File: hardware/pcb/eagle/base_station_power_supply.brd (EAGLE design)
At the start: 30 x 68.5 mm, 17 parts, among them CON1 POWER_JACKPTH, IC1 MB16S-TP

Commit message: Increased width of 24V track
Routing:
- net N$8: track 17.9 -> 22.9 mm
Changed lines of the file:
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@@
 </signal>
 <signal name="+24V">
-<wire x1="2.5" y1="8.8" x2="2.5" y2="40" width="1.016" layer="16"/>
-<wire x1="2.5" y1="8.8" x2="5.5" y2="8.8" width="1.016" layer="16"/>
+<wire x1="2.5" y1="8.8" x2="2.5" y2="44.5" width="2.1844" layer="16"/>
+<wire x1="2.5" y1="8.8" x2="5.5" y2="8.8" width="2.1844" layer="16"/>
 <contactref element="IC1" pad="+"/>
 <contactref element="D1" pad="C"/>
 <contactref element="C4" pad="1"/>
 <contactref element="C1" pad="+"/>
-<wire x1="5.5" y1="8.8" x2="26.84" y2="8.8" width="1.016" layer="16"/>
+<wire x1="5.5" y1="8.8" x2="26.84" y2="8.8" width="2.1844" layer="16"/>
 <wire x1="18" y1="13.1" x2="14" y2="13.1" width="1.016" layer="16"/>
 <contactref element="F1" pad="2"/>
@@
 <wire x1="14" y1="13.1" x2="9.5" y2="13.1" width="1.016" layer="16"/>
 <wire x1="9.5" y1="13.1" x2="9.5" y2="13.05" width="1.016" layer="16"/>
-<wire x1="22.8" y1="52.45" x2="22.8" y2="49.5" width="0.8128" layer="16"/>
-<wire x1="22.8" y1="49.5" x2="20.3" y2="47" width="0.8128" layer="16"/>
-<wire x1="20.3" y1="47" x2="5" y2="47" width="0.8128" layer="16"/>
-<wire x1="5" y1="47" x2="2.5" y2="44.5" width="0.8128" layer="16"/>
-<wire x1="2.5" y1="44.5" x2="2.5" y2="40" width="0.8128" layer="16"/>
+<wire x1="22.8" y1="52.45" x2="22.8" y2="50.5" width="0.8128" layer="16"/>
+<wire x1="22.8" y1="50.5" x2="22.8" y2="49" width="2.1844" layer="16"/>
+<wire x1="22.8" y1="49" x2="20.8" y2="47" width="2.1844" layer="16"/>
+<wire x1="20.8" y1="47" x2="5" y2="47" width="2.1844" layer="16"/>
+<wire x1="5" y1="47" x2="2.5" y2="44.5" width="2.1844" layer="16"/>
 <contactref element="CON2" pad="1"/>
 <contactref element="CON4" pad="3"/>
-<wire x1="28.5" y1="10.96" x2="26.84" y2="8.8" width="1.016" layer="16"/>
+<wire x1="28.5" y1="10.96" x2="26.84" y2="8.8" width="1.4224" layer="16"/>
 <wire x1="22.8" y1="52.45" x2="24" y2="52.45" width="0.8128" layer="16"/>
-<wire x1="24" y1="52.45" x2="25" y2="53.45" width="0.8128" layer="16"/>
-<wire x1="25" y1="53.45" x2="25" y2="56.54" width="0.8128" layer="16"/>
-<wire x1="25" y1="56.54" x2="26" y2="57.54" width="0.8128" layer="16"/>
-<wire x1="26" y1="57.54" x2="28.5" y2="57.54" width="0.8128" layer="16"/>
+<wire x1="24" y1="52.45" x2="25" y2="53.45" width="1.016" layer="16"/>
+<wire x1="25" y1="53.45" x2="25" y2="56.54" width="1.6764" layer="16"/>
+<wire x1="25" y1="56.54" x2="26" y2="57.54" width="1.6764" layer="16"/>
+<wire x1="26" y1="57.54" x2="28.5" y2="57.54" width="1.27" layer="16"/>
 </signal>
 <signal name="S$41">
@@
 <via x="17.5" y="55" extent="1-16" drill="0.6"/>
 <via x="15" y="52.5" extent="1-16" drill="0.6"/>
-<via x="17.5" y="63" extent="1-16" drill="0.6"/>
-<via x="15" y="63" extent="1-16" drill="0.6"/>
-<via x="12.5" y="63" extent="1-16" drill="0.6"/>
 <via x="10" y="63" extent="1-16" drill="0.6"/>
 <via x="7.5" y="60.5" extent="1-16" drill="0.6"/>
@@
 <via x="2.5" y="55.5" extent="1-16" drill="0.6"/>
 <via x="2.5" y="53" extent="1-16" drill="0.6"/>
-<via x="20" y="63" extent="1-16" drill="0.6"/>
 <via x="27.5" y="29" extent="1-16" drill="0.6"/>
 <via x="27.5" y="26.5" extent="1-16" drill="0.6"/>
@@
 <contactref element="CON1" pad="GND"/>
 <contactref element="D1A" pad="1"/>
-<wire x1="18.5" y1="60.35" x2="12.55" y2="60.35" width="0.8128" layer="16"/>
-<wire x1="12.55" y1="60.35" x2="7.7" y2="55.5" width="0.8128" layer="16"/>
-<wire x1="22.8" y1="58.55" x2="21" y2="60.35" width="0.8128" layer="16"/>
-<wire x1="21" y1="60.35" x2="18.5" y2="60.35" width="0.8128" layer="16"/>
+<wire x1="18.5" y1="60.35" x2="18.5" y2="62.5" width="0.8128" layer="16"/>
+<wire x1="18.5" y1="62.5" x2="14.7" y2="62.5" width="2.1844" layer="16"/>
+<wire x1="14.7" y1="62.5" x2="7.7" y2="55.5" width="2.1844" layer="16"/>
+<wire x1="22.8" y1="58.55" x2="22.8" y2="60.5" width="1.016" layer="16"/>
+<wire x1="22.8" y1="60.5" x2="20.8" y2="62.5" width="2.1844" layer="16"/>
+<wire x1="20.8" y1="62.5" x2="18.5" y2="62.5" width="2.1844" layer="16"/>
 </signal>
 <signal name="N$2">

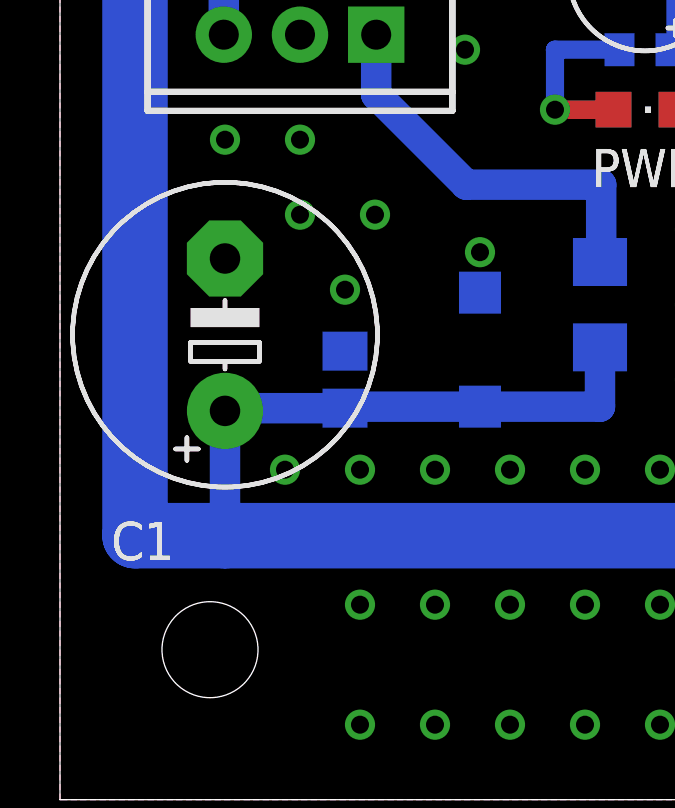
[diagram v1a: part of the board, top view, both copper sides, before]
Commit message: Moved C1 down 1.5mm to increase clearance between capacitor and regulator
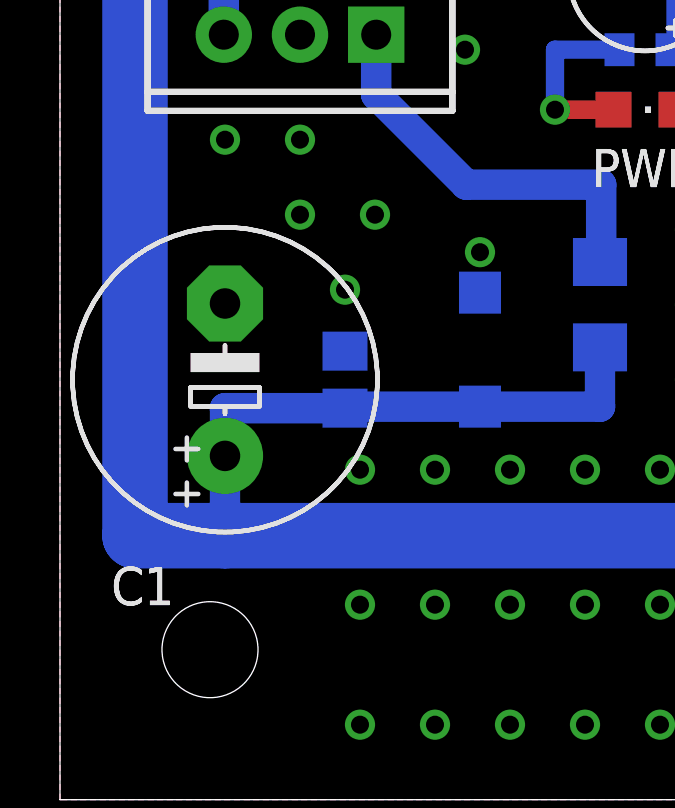
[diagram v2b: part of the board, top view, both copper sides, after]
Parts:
- moved C1 1.50 mm to (5.50, 14.0)
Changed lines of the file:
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@@
 <wire x1="30" y1="68.5" x2="30" y2="0" width="0" layer="20"/>
 <wire x1="30" y1="68.5" x2="0" y2="68.5" width="0" layer="20"/>
-<wire x1="5.499996875" y1="14.357003125" x2="5.499996875" y2="14.611003125" width="0.1524" layer="121"/>
-<wire x1="5.499996875" y1="14.611003125" x2="6.642996875" y2="14.611003125" width="0.1524" layer="121"/>
-<wire x1="6.642996875" y1="14.611003125" x2="6.642996875" y2="15.246003125" width="0.1524" layer="121"/>
-<wire x1="6.642996875" y1="15.246003125" x2="4.356996875" y2="15.246003125" width="0.1524" layer="121"/>
-<wire x1="4.356996875" y1="15.246003125" x2="4.356996875" y2="14.611003125" width="0.1524" layer="121"/>
-<wire x1="4.356996875" y1="14.611003125" x2="5.499996875" y2="14.611003125" width="0.1524" layer="121"/>
-<wire x1="5.499996875" y1="16.135003125" x2="5.499996875" y2="16.643003125" width="0.1524" layer="121"/>
+<wire x1="5.499996875" y1="12.857003125" x2="5.499996875" y2="13.111003125" width="0.1524" layer="121"/>
+<wire x1="5.499996875" y1="13.111003125" x2="6.642996875" y2="13.111003125" width="0.1524" layer="121"/>
+<wire x1="6.642996875" y1="13.111003125" x2="6.642996875" y2="13.746003125" width="0.1524" layer="121"/>
+<wire x1="6.642996875" y1="13.746003125" x2="4.356996875" y2="13.746003125" width="0.1524" layer="121"/>
+<wire x1="4.356996875" y1="13.746003125" x2="4.356996875" y2="13.111003125" width="0.1524" layer="121"/>
+<wire x1="4.356996875" y1="13.111003125" x2="5.499996875" y2="13.111003125" width="0.1524" layer="121"/>
+<wire x1="5.499996875" y1="14.635003125" x2="5.499996875" y2="15.143003125" width="0.1524" layer="121"/>
 <wire x1="3.848996875" y1="11.690003125" x2="4.610996875" y2="11.690003125" width="0.1524" layer="121"/>
 <wire x1="4.229996875" y1="12.071003125" x2="4.229996875" y2="11.309003125" width="0.1524" layer="121"/>
-<circle x="5.499996875" y="15.500003125" radius="5.08" width="0.1524" layer="121"/>
-<rectangle x1="5.182496875" y1="14.928503125" x2="5.817496875" y2="17.214503125" layer="121" rot="R90"/>
-<text x="3.80099375" y="9.2568125" size="1.27" layer="121" font="vector" ratio="10" rot="R180">C1</text>
+<circle x="5.499996875" y="14.000003125" radius="5.08" width="0.1524" layer="121"/>
+<rectangle x1="5.182496875" y1="13.428503125" x2="5.817496875" y2="15.714503125" layer="121" rot="R90"/>
+<text x="3.80099375" y="7.7568125" size="1.27" layer="121" font="vector" ratio="10" rot="R180">C1</text>
 <wire x1="20.769996875" y1="25.72200625" x2="20.261996875" y2="25.72200625" width="0.1524" layer="121"/>
 <wire x1="20.515996875" y1="25.97600625" x2="20.515996875" y2="25.46800625" width="0.1524" layer="121"/>
@@
 <attribute name="VALUE" x="18.865" y="27.54" size="1.27" layer="28" rot="MR180"/>
 </element>
-<element name="C1" library="rcl" package="E5-10,5" value="100uF" x="5.5" y="15.5" smashed="yes" rot="R90">
-<attribute name="NAME" x="3.801" y="9.2568" size="1.27" layer="25" font="vector" ratio="10" rot="R180"/>
-<attribute name="VALUE" x="8.7258" y="12.3758" size="1.27" layer="27" ratio="10" rot="R90"/>
+<element name="C1" library="rcl" package="E5-10,5" value="100uF" x="5.5" y="14" smashed="yes" rot="R90">
+<attribute name="NAME" x="3.801" y="7.7568" size="1.27" layer="25" font="vector" ratio="10" rot="R180"/>
+<attribute name="VALUE" x="8.7258" y="10.8758" size="1.27" layer="27" ratio="10" rot="R90"/>
 </element>
 <element name="C3" library="rcl" package="E5-10,5" value="10uF" x="8" y="34.25" smashed="yes">
@@
 <wire x1="18" y1="13.1" x2="18" y2="15.078" width="1.016" layer="16"/>
 <wire x1="9.5" y1="13.05" x2="5.5" y2="13.05" width="1.016" layer="16"/>
-<wire x1="5.5" y1="13.05" x2="5.5" y2="12.96" width="1.016" layer="16"/>
-<wire x1="5.5" y1="12.96" x2="5.5" y2="8.8" width="1.016" layer="16"/>
+<wire x1="5.5" y1="13.05" x2="5.5" y2="11.46" width="1.016" layer="16"/>
+<wire x1="5.5" y1="11.46" x2="5.5" y2="8.8" width="1.016" layer="16"/>
 <wire x1="14" y1="13.1" x2="9.5" y2="13.1" width="1.016" layer="16"/>
 <wire x1="9.5" y1="13.1" x2="9.5" y2="13.05" width="1.016" layer="16"/>
@@
 <via x="12.5" y="11" extent="1-16" drill="0.6"/>
 <via x="10" y="11" extent="1-16" drill="0.6"/>
-<via x="7.5" y="11" extent="1-16" drill="0.6"/>
 <via x="20" y="6.5" extent="1-16" drill="0.6"/>
 <via x="17.5" y="6.5" extent="1-16" drill="0.6"/>
